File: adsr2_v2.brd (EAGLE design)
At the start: 99.4 x 29.2 mm, 57 parts, among them IC1 LM324D, IC2 4052D, SW1_TIME TL2285 L, SW2_TRIG TL2285 L, T1 BC847, T2 BC857, T3 BC857, T4 BC847, T5 BC857

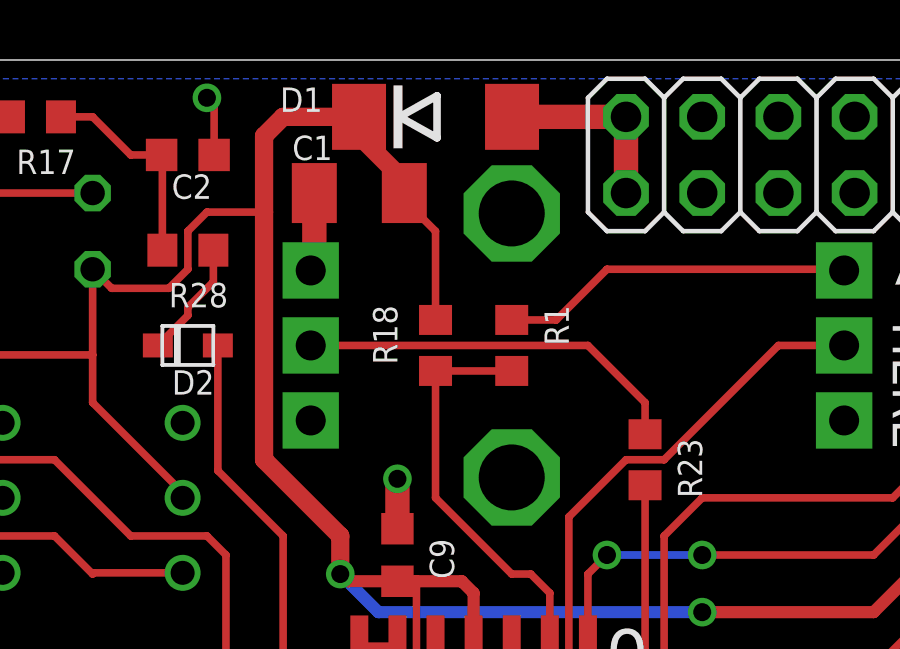
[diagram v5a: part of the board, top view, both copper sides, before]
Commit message: Moved power diode and cap a bit to make it easier to solder components around PSU header/release pot.
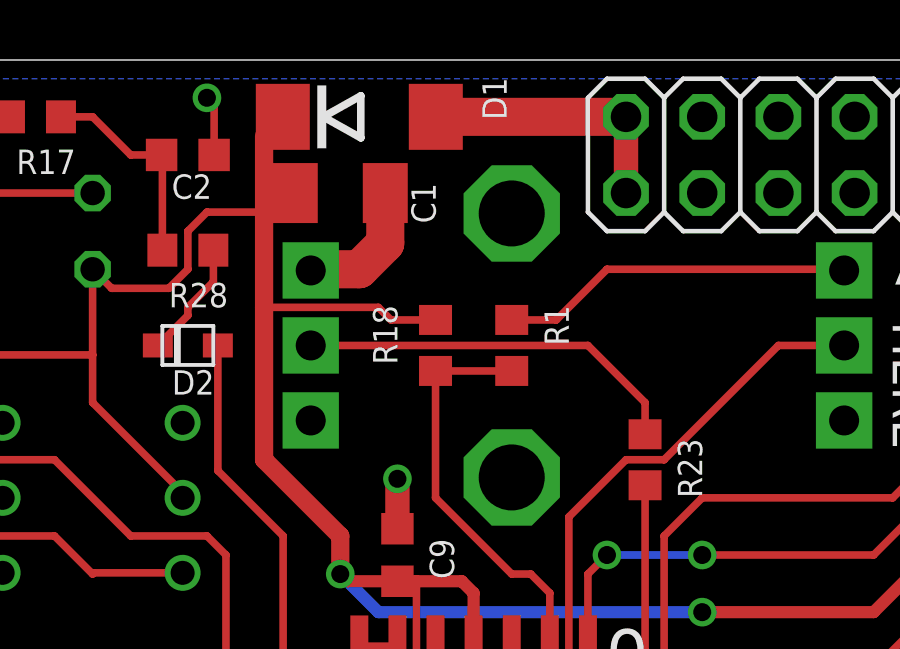
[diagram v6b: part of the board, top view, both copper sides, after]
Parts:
- moved D1 2.54 mm to (35.6, 38.1)
- moved C1 0.64 mm to (34.9, 35.6), turned to 0 degrees
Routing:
- net +12V: track 186.7 -> 183.6 mm
- net N$3: track 6.34 -> 8.88 mm
- net GND: track 61.3 -> 63.2 mm
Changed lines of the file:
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@@
 </autorouter>
 <elements>
-<element name="C1" library="rcl" package="C1206K" value="10u 16V" x="35.56" y="35.56" smashed="yes" rot="R180">
-<attribute name="NAME" x="33.325" y="36.66" size="0.8128" layer="25" font="vector"/>
+<element name="C1" library="rcl" package="C1206K" value="10u 16V" x="34.925" y="35.56" smashed="yes">
+<attribute name="NAME" x="37.295" y="35.89" size="0.8128" layer="25" font="vector" rot="R270"/>
 </element>
 <element name="C11" library="rcl" package="C1206K" value="4u7" x="60.96" y="17.78" smashed="yes" rot="R270">
@@
 <attribute name="NAME" x="38.72" y="22.695" size="0.8128" layer="25" font="vector" rot="R90"/>
 </element>
-<element name="D1" library="diode" package="DO214AA" value="1N4004 equiv" x="38.1" y="38.1" smashed="yes">
-<attribute name="NAME" x="32.92" y="38.266" size="0.8128" layer="25" font="vector" ratio="10"/>
+<element name="D1" library="diode" package="DO214AA" value="1N4004 equiv" x="35.56" y="38.1" smashed="yes">
+<attribute name="NAME" x="40.474" y="38" size="0.8128" layer="25" font="vector" ratio="10" rot="R90"/>
 </element>
 <element name="D3" library="adafruit" package="SOD-323F" value="1N4148" x="88.9" y="23.495" smashed="yes" rot="R270">
@@
 <contactref element="D1" pad="A"/>
 <wire x1="44.45" y1="38.1" x2="44.45" y2="35.56" width="0.8128" layer="1"/>
-<wire x1="44.45" y1="38.1" x2="40.65" y2="38.1" width="0.8128" layer="1"/>
+<wire x1="44.45" y1="38.1" x2="38.11" y2="38.1" width="1.27" layer="1"/>
 </signal>
 <signal name="GND">
@@
 <via x="38.735" y="13.335" extent="1-16" drill="0.6" shape="square"/>
 <via x="36.83" y="26.035" extent="1-16" drill="0.6" shape="square"/>
-<wire x1="34.06" y1="35.56" x2="34.06" y2="33.1" width="0.8128" layer="1"/>
-<wire x1="34.06" y1="33.1" x2="33.94" y2="32.98" width="0.8128" layer="1"/>
 <wire x1="16.51" y1="12.55" x2="18.9" y2="12.55" width="0.254" layer="1"/>
 <wire x1="36.83" y1="24.37" x2="36.83" y2="26.035" width="0.8128" layer="1"/>
@@
 <wire x1="30.72" y1="36.83" x2="30.72" y2="38.495" width="0.254" layer="1"/>
 <wire x1="30.72" y1="38.495" x2="30.48" y2="38.735" width="0.254" layer="1"/>
+<wire x1="36.425" y1="35.56" x2="36.425" y2="33.885" width="1.27" layer="1"/>
+<wire x1="36.425" y1="33.885" x2="35.56" y2="33.02" width="1.27" layer="1"/>
+<wire x1="35.56" y1="33.02" x2="33.98" y2="33.02" width="1.27" layer="1"/>
+<wire x1="33.98" y1="33.02" x2="33.94" y2="32.98" width="1.27" layer="1"/>
 </signal>
 <signal name="+12V">
@@
 <wire x1="39.37" y1="22.225" x2="39.37" y2="20.38" width="0.4064" layer="1"/>
 <wire x1="34.925" y1="24.13" x2="32.385" y2="26.67" width="0.6096" layer="1"/>
-<wire x1="32.385" y1="26.67" x2="32.385" y2="34.925" width="0.6096" layer="1"/>
+<wire x1="32.385" y1="26.67" x2="32.385" y2="31.75" width="0.6096" layer="1"/>
 <contactref element="SW_MANUAL" pad="5"/>
+<wire x1="32.385" y1="31.75" x2="32.385" y2="34.925" width="0.6096" layer="1"/>
 <wire x1="32.385" y1="34.925" x2="32.385" y2="37.465" width="0.6096" layer="1"/>
 <wire x1="18.585" y1="18.735" x2="18.73" y2="18.735" width="0.254" layer="1"/>
@@
 <wire x1="36.195" y1="17.78" x2="37.465" y2="19.05" width="0.254" layer="1"/>
 <wire x1="37.465" y1="19.05" x2="37.465" y2="22.62" width="0.254" layer="1"/>
-<wire x1="32.385" y1="37.465" x2="33.02" y2="38.1" width="0.6096" layer="1"/>
-<wire x1="33.02" y1="38.1" x2="35.55" y2="38.1" width="0.6096" layer="1"/>
-<wire x1="35.55" y1="38.1" x2="35.55" y2="37.475" width="0.6096" layer="1"/>
-<wire x1="35.55" y1="37.475" x2="36.83" y2="36.195" width="0.6096" layer="1"/>
-<wire x1="36.83" y1="36.195" x2="36.83" y2="35.79" width="0.6096" layer="1"/>
-<wire x1="36.83" y1="35.79" x2="37.06" y2="35.56" width="0.6096" layer="1"/>
 <contactref element="T3" pad="E"/>
 <contactref element="LED1" pad="A"/>
@@
 <wire x1="19.685" y1="14.605" x2="19.685" y2="17.78" width="0.254" layer="1"/>
 <wire x1="12.87" y1="30.165" x2="26.67" y2="30.165" width="0.254" layer="1"/>
-<wire x1="37.06" y1="35.56" x2="37.06" y2="35.33" width="0.254" layer="1"/>
-<wire x1="37.06" y1="35.33" x2="38.1" y2="34.29" width="0.254" layer="1"/>
-<wire x1="38.1" y1="34.29" x2="38.1" y2="31.33" width="0.254" layer="1"/>
 <contactref element="IC2" pad="16"/>
 <wire x1="46.99" y1="21.59" x2="52.705" y2="21.59" width="0.4064" layer="1"/>
@@
 <wire x1="29.21" y1="32.385" x2="27.305" y2="32.385" width="0.254" layer="1"/>
 <wire x1="27.305" y1="32.385" x2="26.67" y2="33.02" width="0.254" layer="1"/>
+<wire x1="32.385" y1="34.925" x2="32.79" y2="34.925" width="0.254" layer="1"/>
+<wire x1="32.79" y1="34.925" x2="33.425" y2="35.56" width="0.254" layer="1"/>
+<wire x1="33.01" y1="38.1" x2="33.01" y2="38.09" width="0.254" layer="1"/>
+<wire x1="33.01" y1="38.09" x2="32.385" y2="37.465" width="0.254" layer="1"/>
+<wire x1="38.1" y1="31.33" x2="36.615" y2="31.33" width="0.254" layer="1"/>
+<wire x1="36.615" y1="31.33" x2="36.195" y2="31.75" width="0.254" layer="1"/>
+<wire x1="36.195" y1="31.75" x2="32.385" y2="31.75" width="0.254" layer="1"/>
 </signal>
 <signal name="SUST_LEVEL">

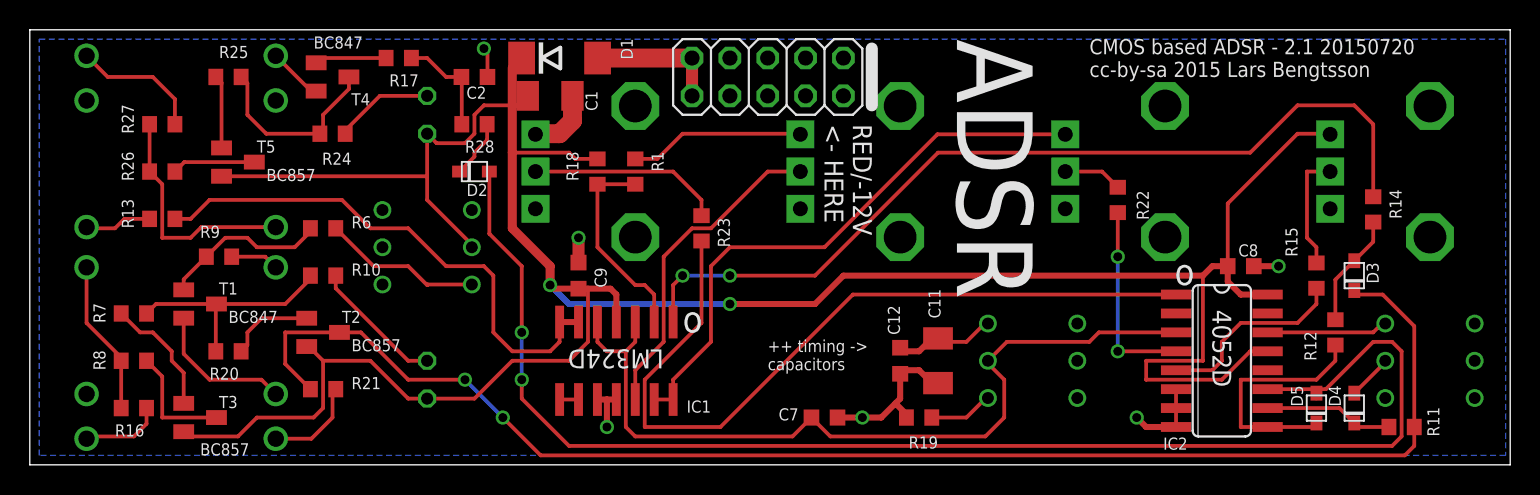
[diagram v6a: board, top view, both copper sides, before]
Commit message: Fixed direction of potentiometers. Added debouncing circuit for manual trig button. Updated date/version label.
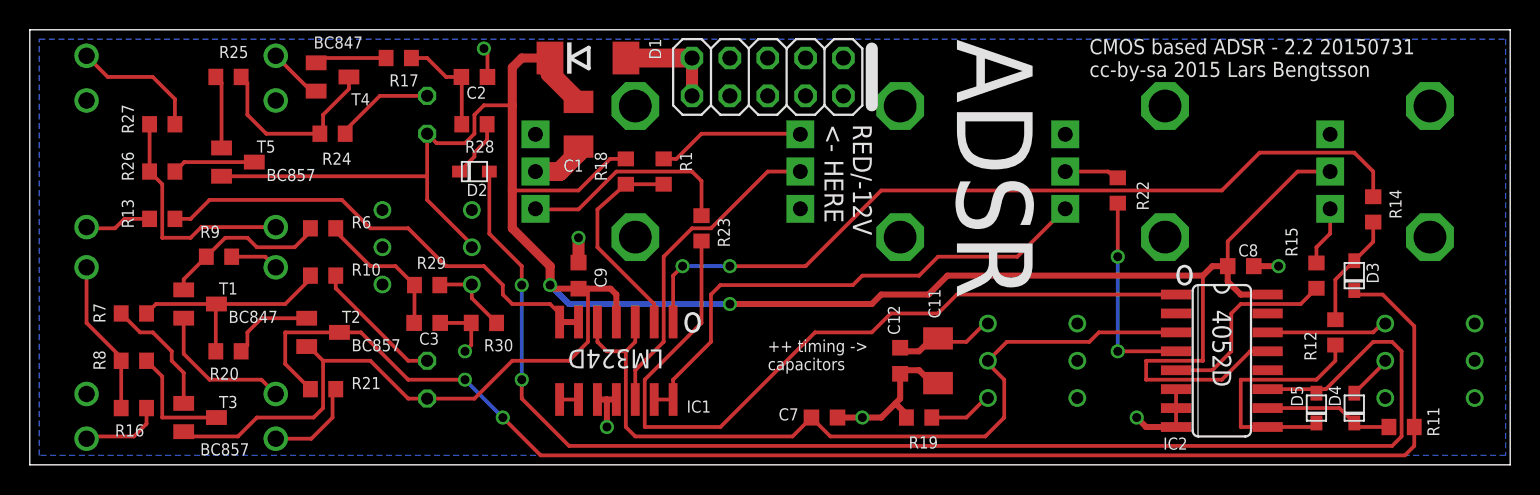
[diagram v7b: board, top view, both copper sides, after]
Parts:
- added C3: 100n, rcl:C0603K
- added R29, R30: 10k, rcl:R0603
- moved C1 2.69 mm to (36.8, 33.7), turned to 270 degrees
- moved D1 1.91 mm to (37.5, 38.1)
- moved R1 1.91 mm to (42.5, 30.5)
- moved R18 1.91 mm to (40.0, 30.5)
- moved R22 0.64 mm to (73.0, 29.2)
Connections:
- removed net N$28 (its old number): R15.1, R5.P$2
- new net N$15: C3.1, R29.2, R6.2
- new net N$25: R15.1, R5.P$3
- net +12V: now also R5.P$2; no longer R5.P$1
- net GND: now also C3.2, R3.P$2, R30.1; no longer R3.P$1
- net N$23: now also R3.P$3; no longer R3.P$2
- net N$4: now also R29.1, R30.2; no longer R6.2
- net N$7: now also R4.P$3; no longer R4.P$1
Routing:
- net N$15: track 0.00 -> 9.54 mm
- net N$28 (its old number): track 7.95 -> 0.00 mm
- net N$4: track 10.7 -> 5.43 mm
- net +12V: track 183.6 -> 188.0 mm
- net PEAK: track 59.9 -> 55.7 mm
- net N$25: track 0.00 -> 4.02 mm
- net N$12: track 35.7 -> 31.8 mm
- net GND: track 63.2 -> 66.6 mm, vias 6 -> 7
- net N$7: track 39.3 -> 36.1 mm
- net N$3: track 8.88 -> 6.98 mm
- net N$26: track 11.8 -> 9.89 mm
- net N$23: track 13.0 -> 14.8 mm
- net N$6: track 13.2 -> 13.9 mm
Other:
- board text added: "CMOS based ADSR - 2.2 20150731 cc-by-sa 2015 Lars Bengtsson"
- board text removed: "CMOS based ADSR - 2.1 20150720 cc-by-sa 2015 Lars Bengtsson"
